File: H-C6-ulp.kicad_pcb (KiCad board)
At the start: 4 copper layers, 50.3 x 33 mm, 76 parts, among them J1 USB_C_Receptacle_USB2.0, J2 AFC24-S24FIC-00, J3 SM02B-SRSS-TB(LF)(SN), J4 SM04B-SRSS-TB_LF__SN_, Q1 Si1308, Q2 Si2301CDS, SW1 SW_Push_Dual, SW2 SW_Push_Dual, U1 ESP32-C6, U2 SGM6029CYG/TR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

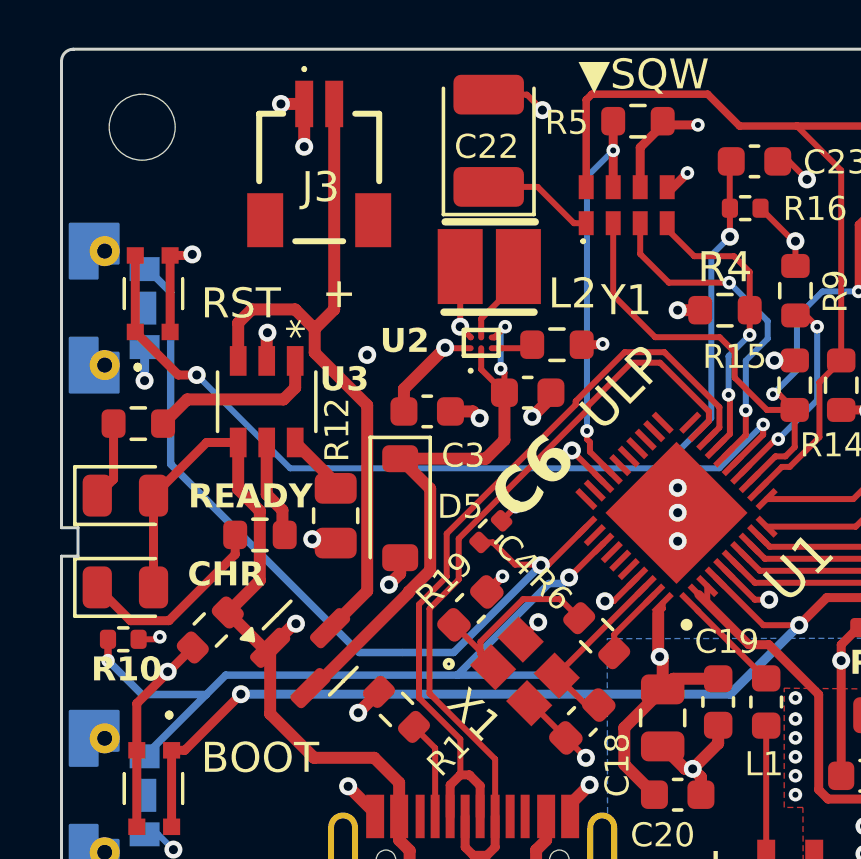
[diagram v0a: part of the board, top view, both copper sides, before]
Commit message: Add superCAP as RTC backup
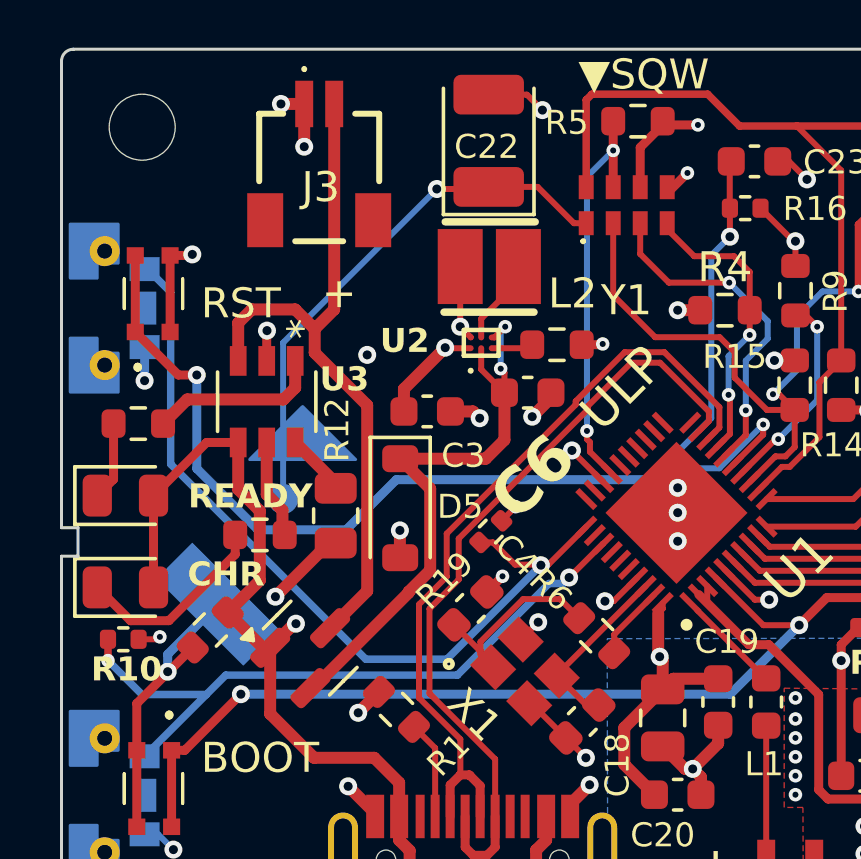
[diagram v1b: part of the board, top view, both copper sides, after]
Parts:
- added C24: superCAP, footprints:superCAP-XH414HG, B.Cu at (124.5, 64.3)
- C22: value C_Polarized 100uF -> C 100uF
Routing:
- net VDD_RTC: track 3.75 -> 17.9 mm, vias 0 -> 1
- net GND: track 73.9 -> 78.9 mm
- net BOOT: track 38.9 -> 42.5 mm
- net SW20: track 25.6 -> 22.7 mm
- net VBUS: track 38.1 -> 39.1 mm

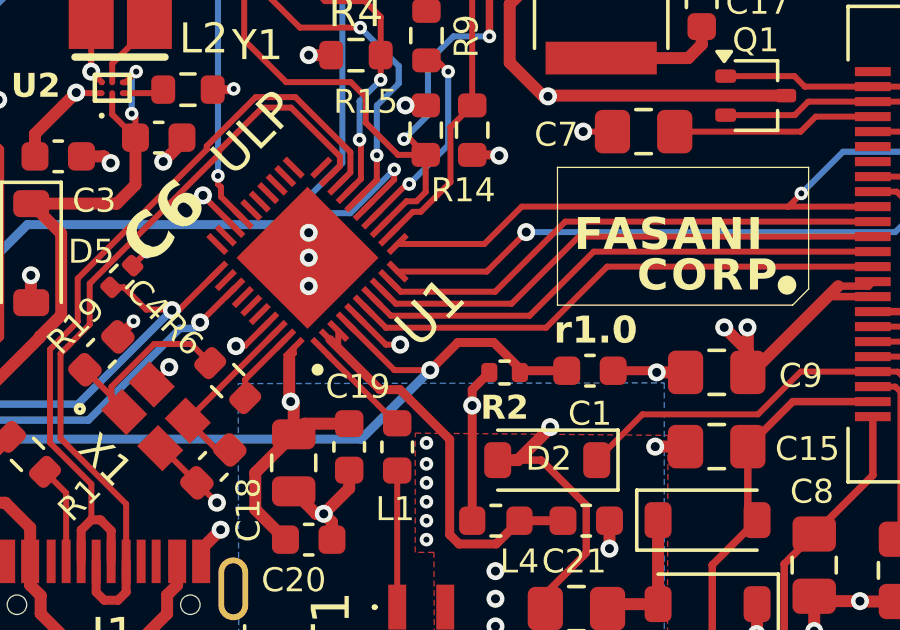
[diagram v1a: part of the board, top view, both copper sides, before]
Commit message: Fix #2 Thanks @Uspizig
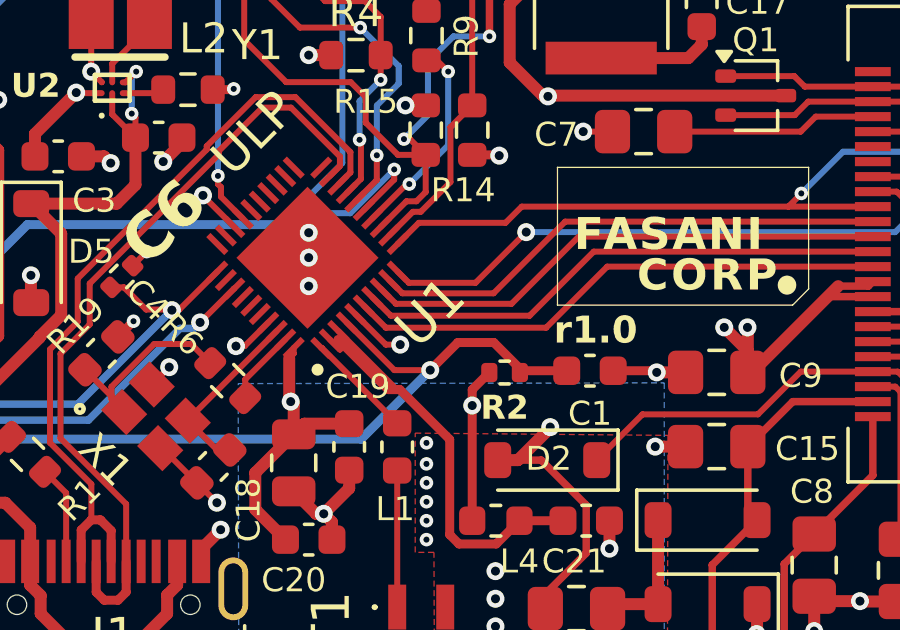
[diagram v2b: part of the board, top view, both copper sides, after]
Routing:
- net Net-(C21-Pad2): track 13.3 -> 15.8 mm
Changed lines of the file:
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@@
     (property "Sheetfile" "H-C6-ulp.kicad_sch")
     (property "Sheetname" "")
-    (attr smd)
+    (attr smd exclude_from_pos_files exclude_from_bom)
     (fp_text reference "U6" (at 0 4.87 90) (layer "B.SilkS") hide
         (effects (font (size 1 1) (thickness 0.15)) (justify mirror))
@@
     (property "Sheetfile" "H-C6-ulp.kicad_sch")
     (property "Sheetname" "")
-    (attr smd)
+    (attr smd exclude_from_pos_files exclude_from_bom)
     (fp_text reference "U4" (at 0 4.87 90) (layer "B.SilkS") hide
         (effects (font (size 1 1) (thickness 0.15)) (justify mirror))
@@
     (property "Sheetfile" "H-C6-ulp.kicad_sch")
     (property "Sheetname" "")
-    (attr smd)
+    (attr smd exclude_from_pos_files exclude_from_bom)
     (fp_text reference "U5" (at 0 4.87 90) (layer "B.SilkS") hide
         (effects (font (size 1 1) (thickness 0.15)) (justify mirror))
@@
     (property "ki_description" "Polarized capacitor")
     (property "ki_keywords" "cap capacitor")
-    (attr through_hole)
+    (attr through_hole exclude_from_pos_files exclude_from_bom)
     (fp_text reference "C24" (at 0.2 0.05 315) (layer "B.SilkS")
         (effects (font (size 1 1) (thickness 0.15)) (justify mirror))
@@
   (segment (start 146.8 57.75) (end 146.725 57.675) (width 0.2) (layer "In1.Cu") (net 20))
   (segment (start 146.8 68.7) (end 146.8 57.75) (width 0.2) (layer "In1.Cu") (net 20))
-  (segment (start 141.789686 67.45) (end 141.124516 67.45) (width 0.3) (layer "F.Cu") (net 21))
   (segment (start 143.760314 72.595) (end 143.45 72.284686) (width 0.3) (layer "F.Cu") (net 21))
+  (segment (start 139.452081 65.777565) (end 139.790469 66.115953) (width 0.2) (layer "F.Cu") (net 21))
+  (segment (start 141.4 67.45) (end 139.727565 65.777565) (width 0.3) (layer "F.Cu") (net 21))
+  (segment (start 139.790469 66.115953) (end 139.791422 66.115) (width 0.2) (layer "F.Cu") (net 21))
   (segment (start 143.45 69.110314) (end 141.789686 67.45) (width 0.3) (layer "F.Cu") (net 21))
   (segment (start 145 72.595) (end 143.760314 72.595) (width 0.3) (layer "F.Cu") (net 21))
   (segment (start 145.775 71.82) (end 145 72.595) (width 0.3) (layer "F.Cu") (net 21))
   (segment (start 143.45 72.284686) (end 143.45 69.110314) (width 0.3) (layer "F.Cu") (net 21))
-  (segment (start 139.734924 65.494722) (end 139.734924 66.060408) (width 0.2) (layer "F.Cu") (net 21))
   (segment (start 147.225 71.82) (end 145.775 71.82) (width 0.3) (layer "F.Cu") (net 21))
-  (segment (start 141.124516 67.45) (end 139.452081 65.777565) (width 0.3) (layer "F.Cu") (net 21))
+  (segment (start 141.690202 67.45) (end 141.789686 67.45) (width 0.2) (layer "F.Cu") (net 21))
+  (segment (start 139.734924 65.494722) (end 141.690202 67.45) (width 0.2) (layer "F.Cu") (net 21))
+  (segment (start 141.789686 67.45) (end 141.4 67.45) (width 0.3) (layer "F.Cu") (net 21))
   (segment (start 135.7 53.4) (end 135.29 53.4) (width 0.2) (layer "F.Cu") (net 22))
   (segment (start 130.72 52.26) (end 132.38 52.26) (width 0.2) (layer "F.Cu") (net 22))
@@
   (segment (start 141.488998 64.986054) (end 146.113946 64.986054) (width 0.2) (layer "F.Cu") (net 33))
   (segment (start 140.866295 64.363352) (end 141.488998 64.986054) (width 0.2) (layer "F.Cu") (net 33))
+  (segment (start 145.51 64.59) (end 141.658628 64.59) (width 0.2) (layer "F.Cu") (net 34))
+  (segment (start 147.75 62.35) (end 145.51 64.59) (width 0.2) (layer "F.Cu") (net 34))
   (segment (start 157.5544 62.35) (end 147.75 62.35) (width 0.2) (layer "F.Cu") (net 34))
-  (segment (start 141.654683 64.586054) (end 141.149137 64.080509) (width 0.2) (layer "F.Cu") (net 34))
-  (segment (start 147.75 62.35) (end 145.513946 64.586054) (width 0.2) (layer "F.Cu") (net 34))
-  (segment (start 145.513946 64.586054) (end 141.654683 64.586054) (width 0.2) (layer "F.Cu") (net 34))
-  (segment (start 144.963946 64.186054) (end 147.300001 61.849999) (width 0.2) (layer "F.Cu") (net 35))
+  (segment (start 141.658628 64.59) (end 141.149137 64.080509) (width 0.2) (layer "F.Cu") (net 34))
+  (segment (start 141.43198 63.797666) (end 141.874314 64.24) (width 0.2) (layer "F.Cu") (net 35))
   (segment (start 147.300001 61.849999) (end 157.5544 61.849999) (width 0.2) (layer "F.Cu") (net 35))
-  (segment (start 141.820368 64.186054) (end 144.963946 64.186054) (width 0.2) (layer "F.Cu") (net 35))
-  (segment (start 141.43198 63.797666) (end 141.820368 64.186054) (width 0.2) (layer "F.Cu") (net 35))
+  (segment (start 144.91 64.24) (end 147.300001 61.849999) (width 0.2) (layer "F.Cu") (net 35))
+  (segment (start 141.874314 64.24) (end 144.91 64.24) (width 0.2) (layer "F.Cu") (net 35))
   (segment (start 155.17 60.92) (end 154.74 61.35) (width 0.2) (layer "F.Cu") (net 36))
+  (segment (start 142.42 61.89) (end 145.31 61.89) (width 0.2) (layer "F.Cu") (net 36))
   (segment (start 164.28 71.02) (end 164.28 70.52) (width 0.2) (layer "F.Cu") (net 36))
+  (segment (start 141.714823 62.595177) (end 142.42 61.89) (width 0.2) (layer "F.Cu") (net 36))
+  (segment (start 145.31 61.89) (end 145.85 61.35) (width 0.2) (layer "F.Cu") (net 36))
   (segment (start 155.17 60.91) (end 155.17 60.92) (width 0.2) (layer "F.Cu") (net 36))
-  (segment (start 144.604415 62.595585) (end 145.85 61.35) (width 0.2) (layer "F.Cu") (net 36))
+  (segment (start 141.714823 62.595585) (end 141.714823 62.595177) (width 0.2) (layer "F.Cu") (net 36))
   (segment (start 164.28 70.52) (end 164.26 70.5) (width 0.2) (layer "F.Cu") (net 36))
-  (segment (start 141.714823 62.595585) (end 144.604415 62.595585) (width 0.2) (layer "F.Cu") (net 36))
   (segment (start 145.85 61.35) (end 154.74 61.35) (width 0.2) (layer "F.Cu") (net 36))
   (segment (start 154.74 61.35) (end 157.5544 61.35) (width 0.2) (layer "F.Cu") (net 36))
@@
   (segment (start 164.28 73.27) (end 164.28 71.02) (width 0.2) (layer "B.Cu") (net 36))
   (segment (start 159 61.5) (end 158.350001 60.850001) (width 0.2) (layer "F.Cu") (net 37))
-  (segment (start 141.714823 63.514823) (end 144.685177 63.514823) (width 0.2) (layer "F.Cu") (net 37))
+  (segment (start 142.09 63.89) (end 144.31 63.89) (width 0.2) (layer "F.Cu") (net 37))
   (segment (start 158.350001 60.850001) (end 157.5544 60.850001) (width 0.2) (layer "F.Cu") (net 37))
-  (segment (start 144.685177 63.514823) (end 146 62.2) (width 0.2) (layer "F.Cu") (net 37))
+  (segment (start 144.31 63.89) (end 146 62.2) (width 0.2) (layer "F.Cu") (net 37))
+  (segment (start 141.714823 63.514823) (end 142.09 63.89) (width 0.2) (layer "F.Cu") (net 37))
   (via (at 146 62.2) (size 0.6) (drill 0.3) (layers "F.Cu" "B.Cu") (net 37))
   (via (at 159 61.5) (size 0.6) (drill 0.3) (layers "F.Cu" "B.Cu") (net 37))
@@
   (segment (start 126.65 57.717956) (end 126.65 56.925) (width 0.4) (layer "F.Cu") (net 43))
   (segment (start 127.162913 66.899587) (end 128.4 65.6625) (width 0.4) (layer "F.Cu") (net 43))
-  (segment (start 141.675 68.575) (end 141.7 68.575) (width 0.2) (layer "F.Cu") (net 46))
-  (segment (start 139.4 66.3) (end 141.675 68.575) (width 0.2) (layer "F.Cu") (net 46))
+  (segment (start 139.169238 66.060408) (end 139.187908 66.060408) (width 0.2) (layer "F.Cu") (net 46))
+  (segment (start 139.187908 66.060408) (end 141.7 68.5725) (width 0.2) (layer "F.Cu") (net 46))
   (segment (start 132.2 56.585) (end 133.44 55.345) (width 0.2) (layer "F.Cu") (net 47))
   (segment (start 132.2 57.2075) (end 132.2 56.585) (width 0.2) (layer "F.Cu") (net 47))

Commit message: Add 1mm TP for coin battery (Passes through regulator also)
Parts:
- added J5: OLED, Connector_PinSocket_2.54mm:PinSocket_1x04_P2.54mm_Vertical, F.Cu at (142.6, 49.8)
- added TP4: COIN BAT +, TestPoint:TestPoint_Pad_D1.0mm, F.Cu at (124.4, 74.2)
- added TP5: COIN BAT -, TestPoint:TestPoint_Pad_D1.0mm, F.Cu at (124.4, 77.4)
- moved C23 3.07 mm to (144.2, 52.4)
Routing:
- net VDD: track 19.8 -> 26.1 mm, vias 2 -> 4
- net GND: track 78.9 -> 82.2 mm
- net /SCL: track 41.0 -> 44.2 mm
- net BOOT: track 42.5 -> 44.1 mm
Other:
- board text added: "-"
- board text added: "COIN_BAT"
- board text added: "GND"
- board text added: "QWIIC"
- board text removed: "QWIIC ▶"
- board text removed: "RESE"

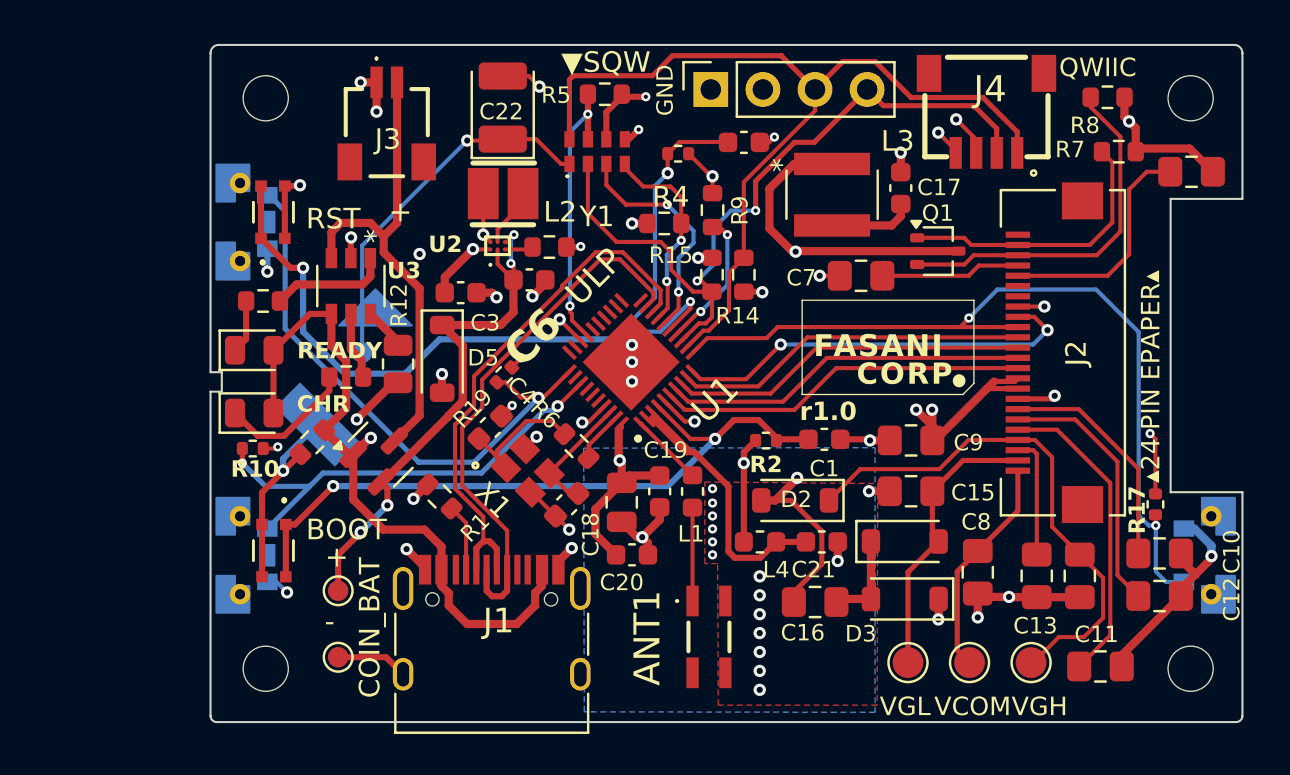
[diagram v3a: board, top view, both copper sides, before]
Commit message: Add QSPI Flash
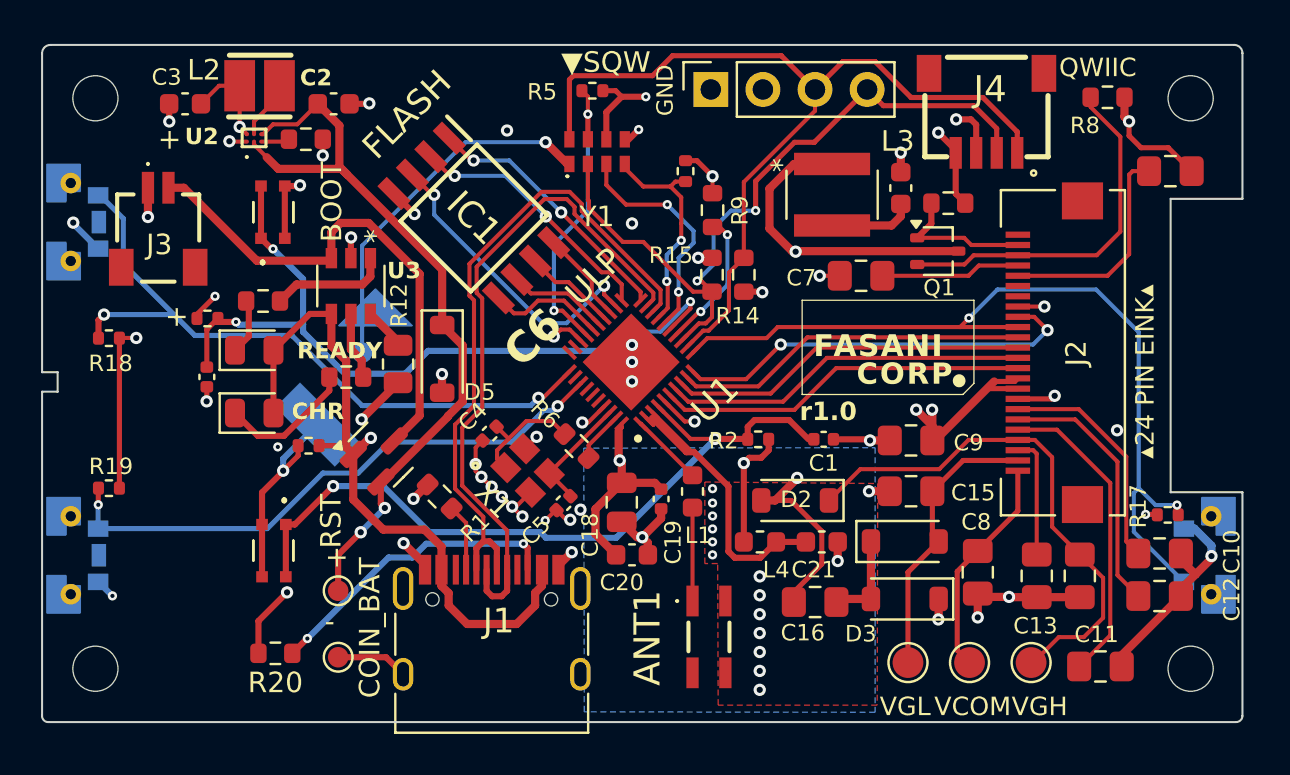
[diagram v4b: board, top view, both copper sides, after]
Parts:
- removed C22: C 100uF, Capacitor_Tantalum_SMD:CP_EIA-3528-21_Kemet-B
- added IC1: W25Q80DVSSIG, footprints:SOIC127P790X216-8N-FLASH, F.Cu at (131.0, 56.0)
- added R20: 5.1k, Resistor_SMD:R_0603_1608Metric, F.Cu at (121.4, 77.2)
- C1, C19, C23, C4, C5: footprint Capacitor_SMD:C_0603_1608Metric -> Capacitor_SMD:C_0402_1005Metric
- R10, R4, R5: footprint Resistor_SMD:R_0603_1608Metric -> Resistor_SMD:R_0402_1005Metric
- moved C23 28.6 mm to (118.0, 63.8), turned to -90 degrees
- moved R16 24.3 mm to (118.1, 60.9), turned to 180 degrees
- moved R19 20.0 mm to (113.3, 69.2), turned to 0 degrees
- moved C3 16.3 mm to (117.0, 50.5)
- moved L2 13.0 mm to (120.6, 49.6)
- moved R3 13.0 mm to (122.9, 52.2)
- moved U2 13.0 mm to (120.3, 52.1)
- moved C2 12.8 mm to (124.2, 50.5)
- moved J3 12.3 mm to (115.7, 56.8)
- moved R18 8.84 mm to (113.3, 61.9)
- moved R7 8.68 mm to (154.2, 55.3)
- moved H1 8.30 mm to (112.6, 50.2)
- moved H3 8.30 mm to (112.6, 78.0)
- moved U4 8.25 mm to (111.9, 56.2)
- moved U6 8.25 mm to (111.9, 72.5)
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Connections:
- J1 pad B5: unconnected-(J1-CC2-PadB5) -> Net-(J1-CC2)
- R18 pad 1: SW20 -> SW18
- R19 pad 1: SW18 -> SW20
- U1 pad 20: unconnected-(U1-SPICS0/GPIO24-Pad20) -> SPICS0
- U1 pad 21: unconnected-(U1-SPIQ/GPIO25-Pad21) -> SPI_D1
- U1 pad 22: unconnected-(U1-SPIWP/GPIO26-Pad22) -> SPI_D2
- U1 pad 23: unconnected-(U1-VDD_SPI/GPIO27-Pad23) -> SPIVDD
- U1 pad 24: unconnected-(U1-SPIHD/GPIO28-Pad24) -> SPI_D3
- U1 pad 25: unconnected-(U1-SPICLK/GPIO29-Pad25) -> SPICLK
- U1 pad 26: unconnected-(U1-SPID/GPIO30-Pad26) -> SPI_D0
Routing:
- net VDD33: track 64.3 -> 99.4 mm, vias 19 -> 20
- net SPI_D2: track 0.00 -> 14.9 mm, vias 0 -> 2
- net Net-(J1-CC2): track 0.00 -> 14.8 mm, vias 0 -> 2
- net SPICS0: track 0.00 -> 12.8 mm, vias 0 -> 2
- net SPI_D1: track 0.00 -> 12.7 mm, vias 0 -> 2
- net VDD: track 26.1 -> 37.9 mm, vias 4 -> 2
- net Net-(Q1-G): track 13.8 -> 7.03 mm
- net GND: track 82.2 -> 88.8 mm, vias 50 -> 58
- net BOOT: track 44.1 -> 37.8 mm
- net /USB_D+: track 26.1 -> 32.3 mm
- net /USB_D-: track 26.0 -> 32.1 mm
- net SW18: track 27.6 -> 33.7 mm, vias 1 -> 2
- net SW20: track 22.7 -> 28.5 mm
- net SPI_D0: track 0.00 -> 5.74 mm
- net +3.3V: track 0.00 -> 5.10 mm
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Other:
- board size 50.3 x 33 mm -> 58.5 x 33 mm
- board text added: "3V3"
- board text added: "FLASH"
- board text added: "Mini TFT I2C"
- board text added: "SCL"
- board text added: "SDA"
- board text added: "▴24 PIN EINK▴"
- board text removed: "▴24 PIN EPAPER▴"
